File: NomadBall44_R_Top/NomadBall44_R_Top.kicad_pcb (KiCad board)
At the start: 2 copper layers, 144.8 x 96.5 mm, 34 parts, among them SW1 SW_Push, SW10 SW_Push, SW11 SW_Push, SW12 SW_Push, SW13 SW_Push, SW14 SW_Push, SW15 SW_Push, SW16 SW_Push, SW17 SW_Push, SW18 SW_Push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

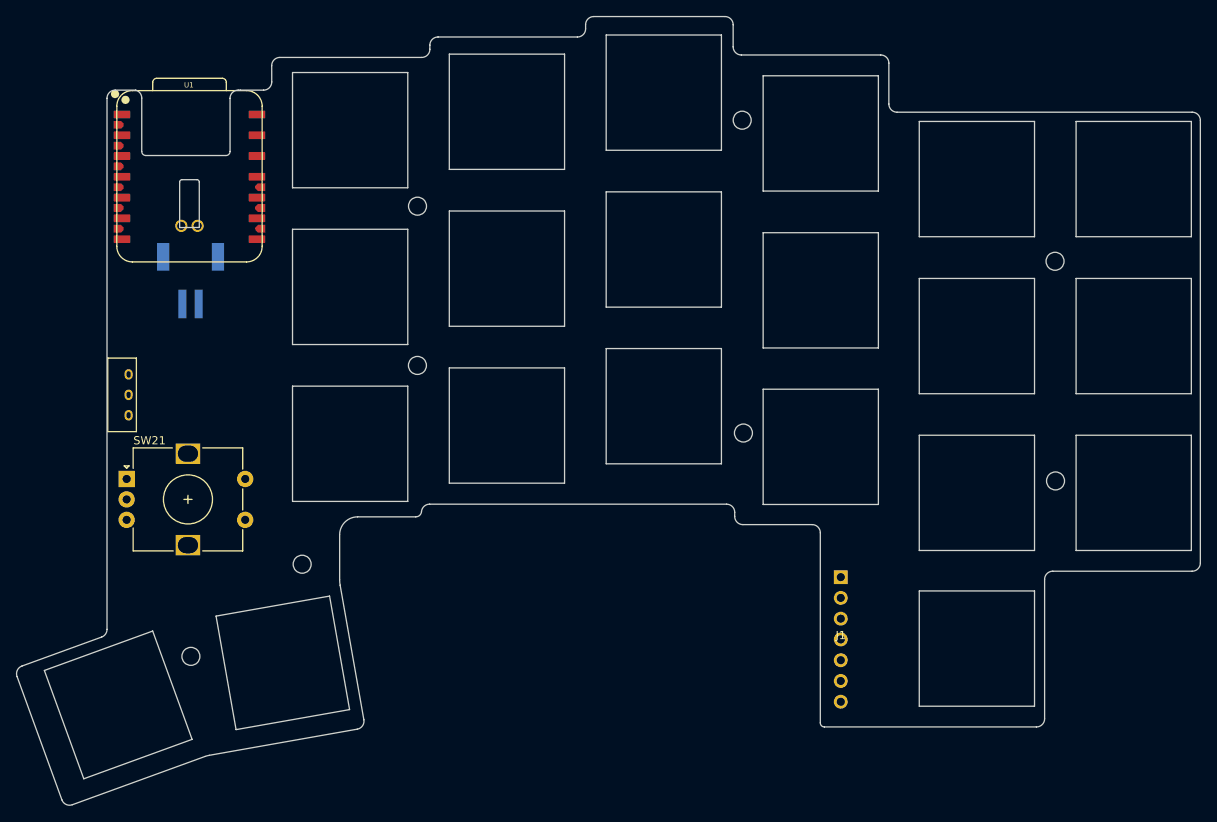
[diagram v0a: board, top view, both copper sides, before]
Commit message: トッププレート用のkicad projectを作成
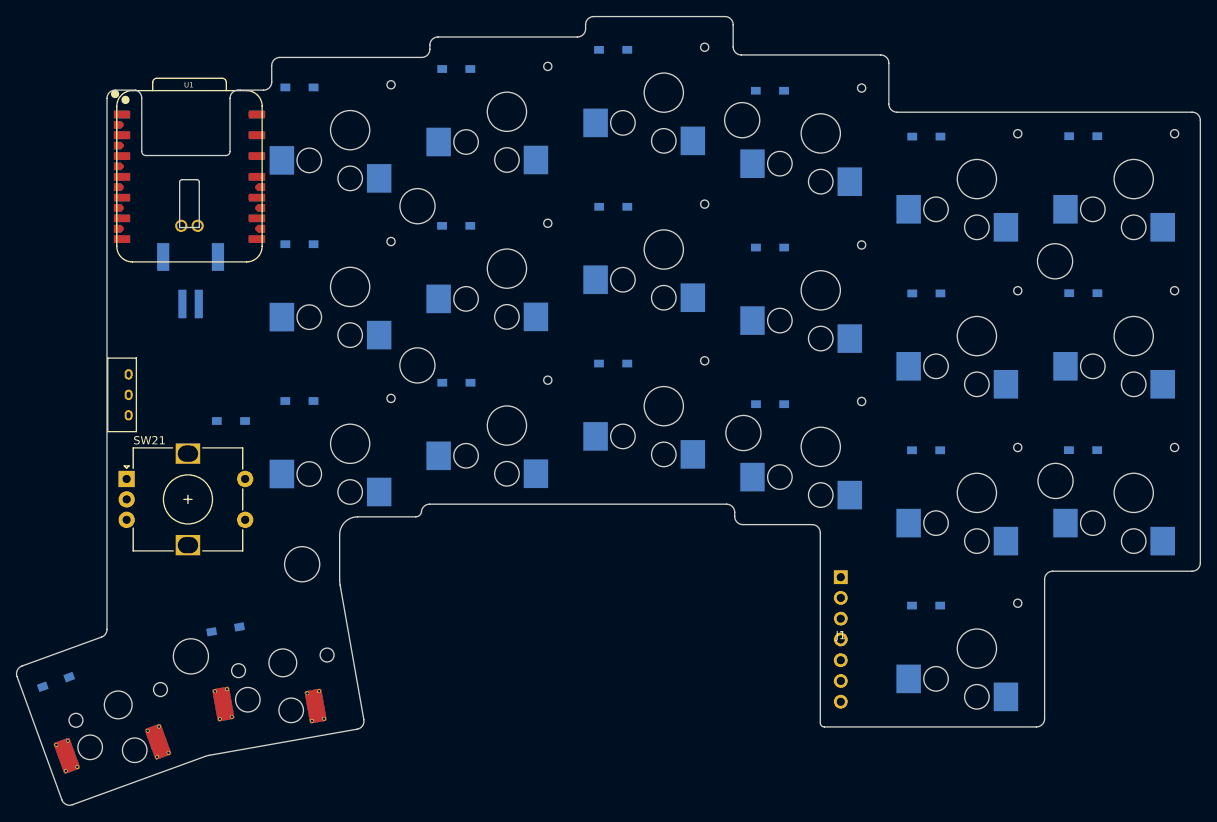
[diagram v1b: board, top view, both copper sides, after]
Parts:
- added D1: D, NomadBall44:Diode_SMD, F.Cu at (106.3, 49.4)
- added D10: D, NomadBall44:Diode_SMD, F.Cu at (163.8, 69.0)
- added D11: D, NomadBall44:Diode_SMD, F.Cu at (183.0, 74.6)
- added D12: D, NomadBall44:Diode_SMD, F.Cu at (202.2, 74.5)
- added D13: D, NomadBall44:Diode_SMD, F.Cu at (106.3, 87.8)
- added D14: D, NomadBall44:Diode_SMD, F.Cu at (125.5, 85.5)
- added D15: D, NomadBall44:Diode_SMD, F.Cu at (144.6, 83.2)
- added D16: D, NomadBall44:Diode_SMD, F.Cu at (163.8, 88.1)
- added D17: D, NomadBall44:Diode_SMD, F.Cu at (182.9, 93.8)
- added D18: D, NomadBall44:Diode_SMD, F.Cu at (202.1, 93.8)
- added D19: D, NomadBall44:Diode_SMD, F.Cu at (76.7, 123.1)
- added D2: D, NomadBall44:Diode_SMD, F.Cu at (125.5, 47.1)
- added D20: D, NomadBall44:Diode_SMD, F.Cu at (97.3, 116.2)
- added D21: D, NomadBall44:Diode_SMD, F.Cu at (97.9, 90.2)
- added D22: D, NomadBall44:Diode_SMD, F.Cu at (182.9, 112.8)
- added D3: D, NomadBall44:Diode_SMD, F.Cu at (144.6, 44.8)
- added D4: D, NomadBall44:Diode_SMD, F.Cu at (163.8, 49.8)
- added D5: D, NomadBall44:Diode_SMD, F.Cu at (183.0, 55.4)
- added D6: D, NomadBall44:Diode_SMD, F.Cu at (202.1, 55.4)
- added D7: D, NomadBall44:Diode_SMD, F.Cu at (106.3, 68.6)
- added D8: D, NomadBall44:Diode_SMD, F.Cu at (125.4, 66.3)
- added D9: D, NomadBall44:Diode_SMD, F.Cu at (144.7, 64.0)
- REF** (x8): value Val** -> MountingHole_4.3mm_M4; footprint NomadBall44:m2_Screw_Hole_EdgeCuts -> MountingHole:MountingHole_4.3mm_M4
- SW1, SW10, SW11, SW12, SW13, SW14, SW15, SW16, SW17, SW18, SW2, SW22, SW3, SW4, SW5, SW6, SW7, SW8, SW9: footprint NomadBall44:SW_Hole_1u -> NomadBall44:Choc_v2_Hotswap_1u
- SW19, SW20: footprint NomadBall44:SW_Hole_1u -> NomadBall44:Kailh_Choc_V1_Hotswap_thin_via

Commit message: トッププレートからダイオードのフットプリントを削除
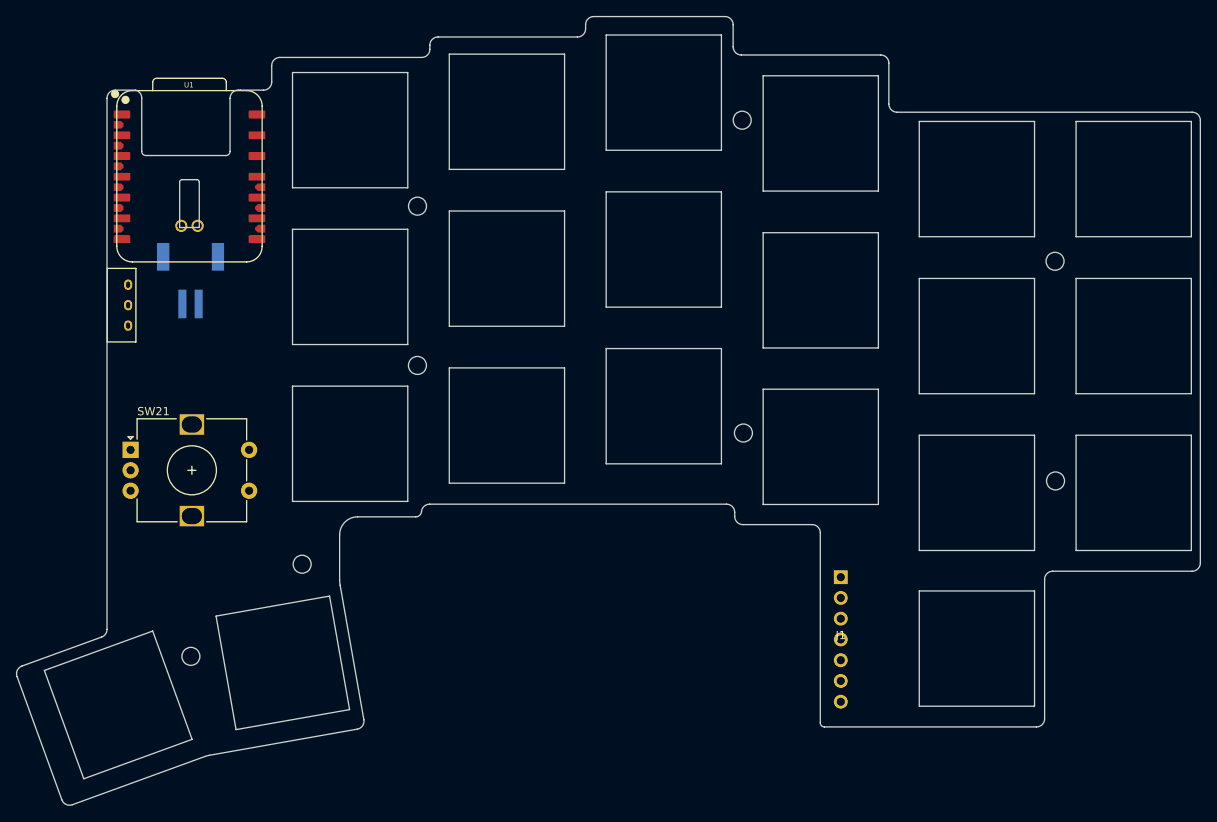
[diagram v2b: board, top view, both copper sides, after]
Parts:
- removed D1, D10, D11, D12, D13, D14, D15, D16, D17, D18, D19, D2, D20, D21, D22, D3, D4, D5, D6, D7, D8, D9: D, NomadBall44:Diode_SMD
- REF** (x8): value MountingHole_4.3mm_M4 -> Val**; footprint MountingHole:MountingHole_4.3mm_M4 -> NomadBall44:m2_Screw_Hole_EdgeCuts
- SW1, SW10, SW11, SW12, SW13, SW14, SW15, SW16, SW17, SW18, SW2, SW22, SW3, SW4, SW5, SW6, SW7, SW8, SW9: footprint NomadBall44:Choc_v2_Hotswap_1u -> NomadBall44:SW_Hole_1u
- SW19, SW20: footprint NomadBall44:Kailh_Choc_V1_Hotswap_thin_via -> NomadBall44:SW_Hole_1u
- moved SW23 11.0 mm to (87.0, 76.0)
- moved SW21 3.59 mm to (88.4, 93.7)
